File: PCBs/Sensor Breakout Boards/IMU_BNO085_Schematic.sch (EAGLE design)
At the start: 6 parts

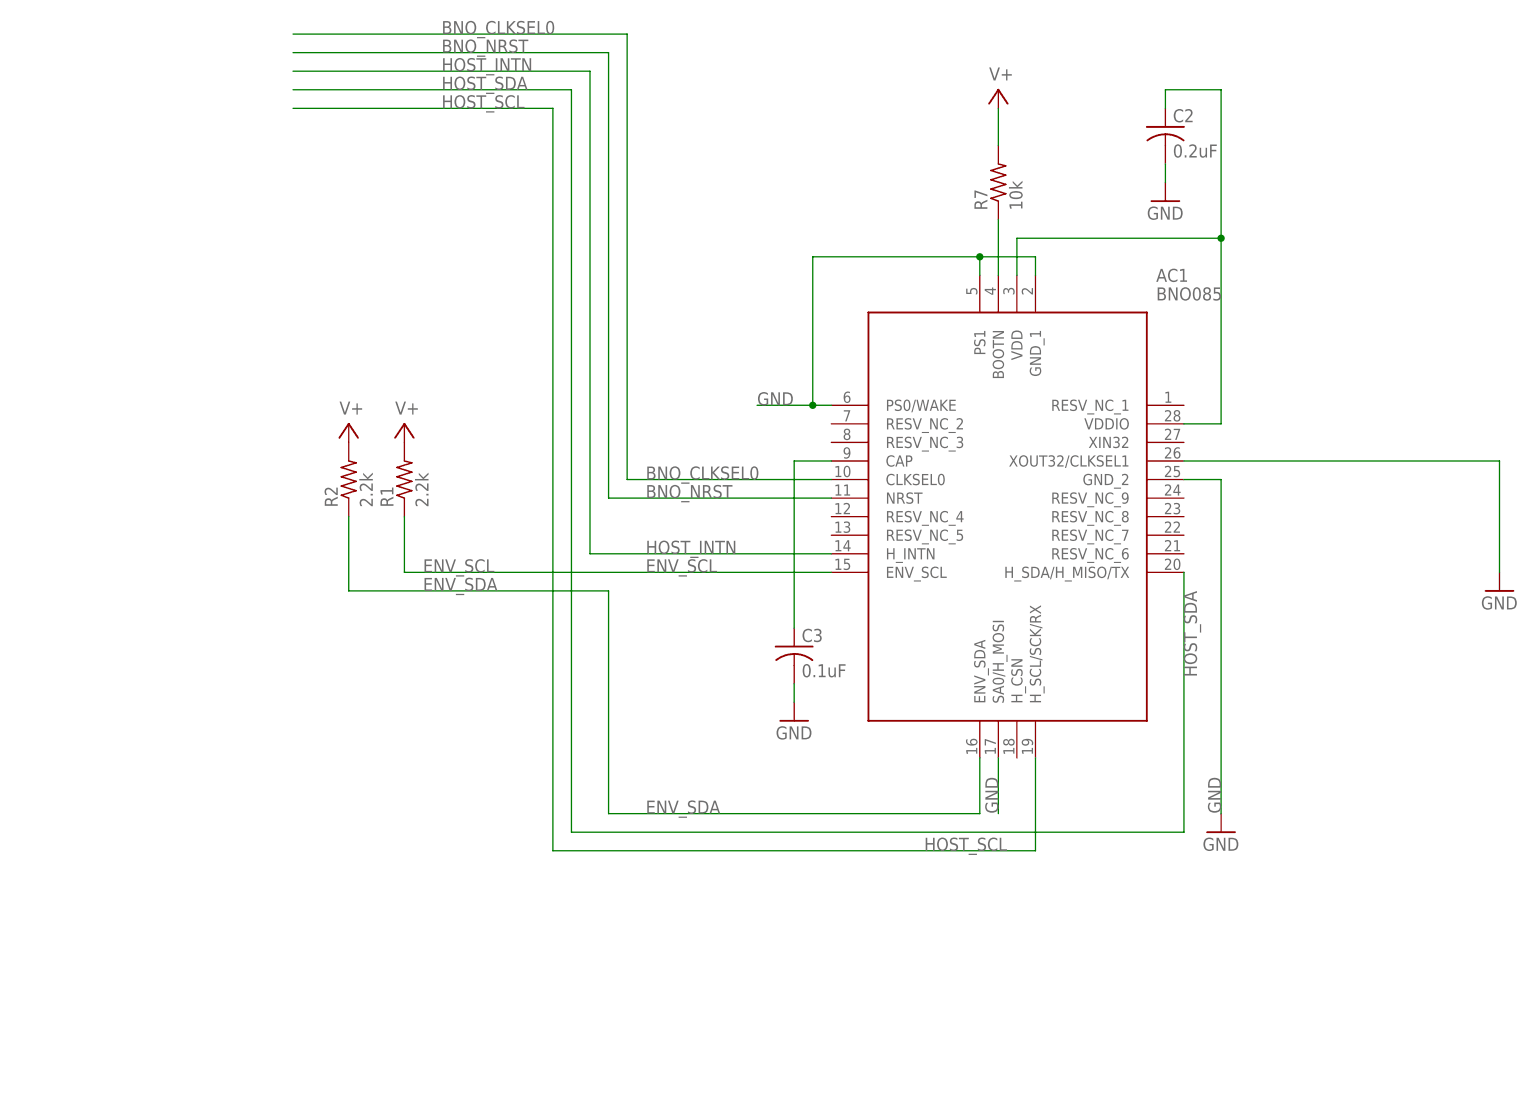
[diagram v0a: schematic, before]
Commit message: Revised IMU schematic and roughed out board
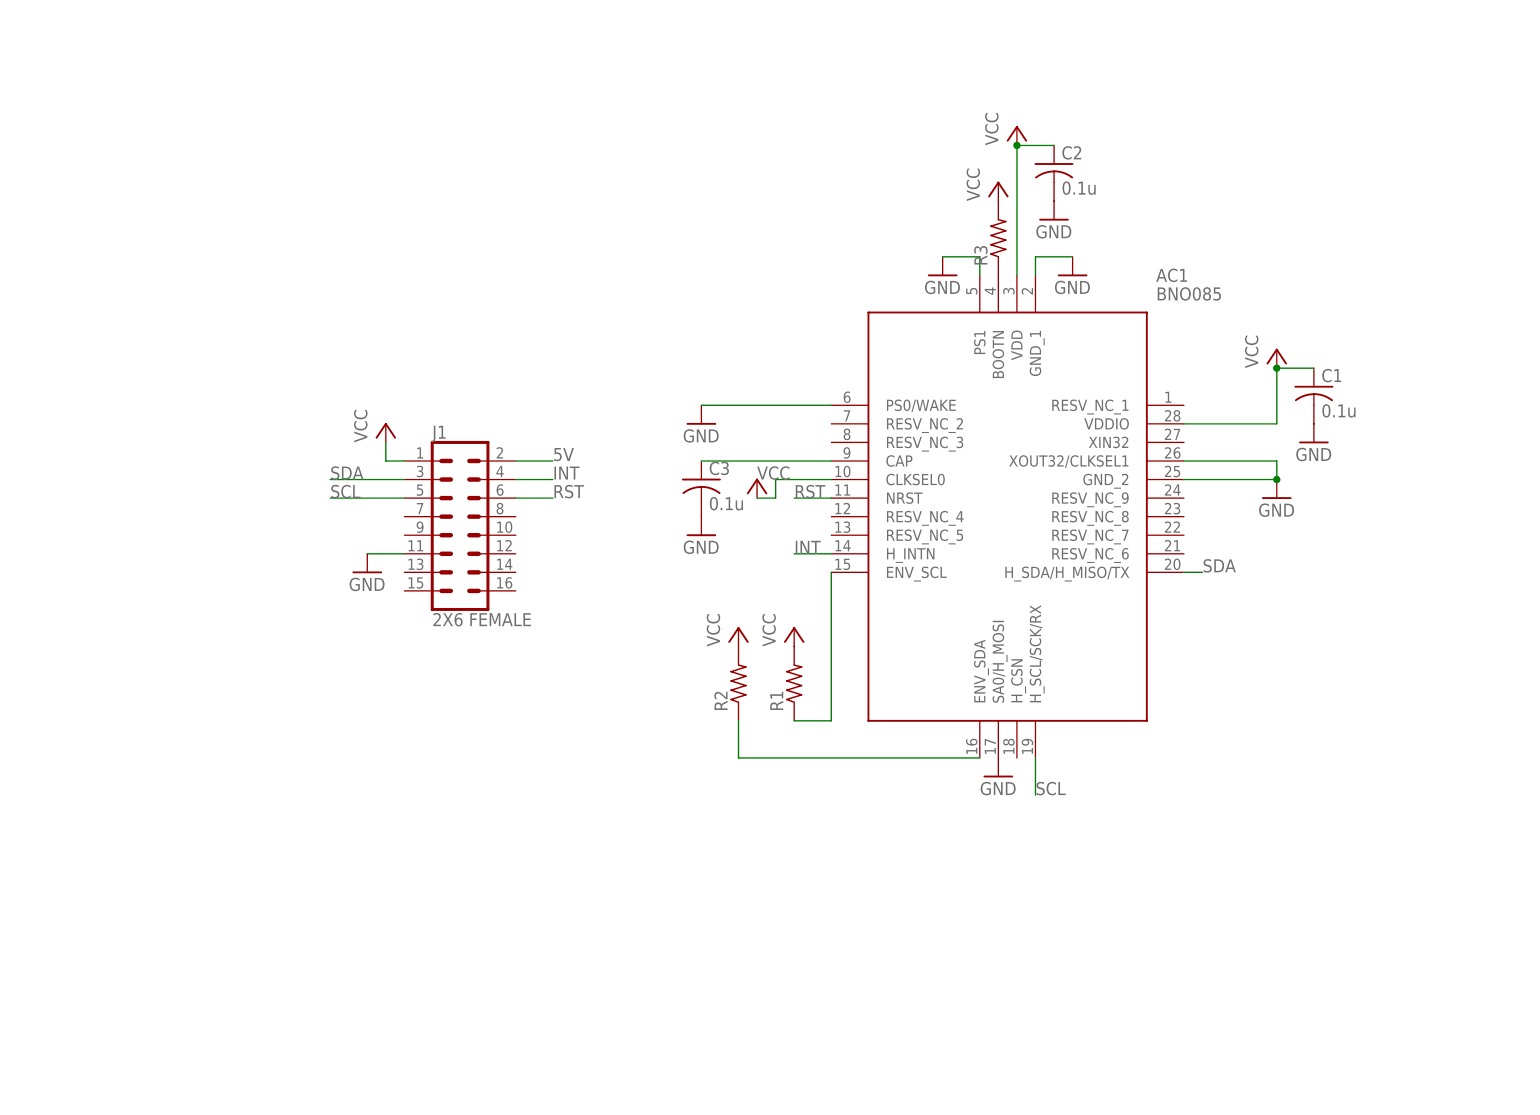
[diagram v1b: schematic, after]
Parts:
- removed R7: 10k, rcl:R-US_M0805
- added C1: 0.1u, RTR Main Library:C-ALL_PACKAGESC1206
- added J1: 2X6 FEMALE, RTR Main Library:SENSOR_BREAKOUTPTH_FEMALE
- added R3: (no value), RTR Main Library:R-ALL_PACKAGESR1206
- C2: value 0.2uF -> 0.1u; device rcl:C-US025-024X044 -> RTR Main Library:C-ALL_PACKAGESC1206
- C3: value 0.1uF -> 0.1u; device rcl:C-US025-024X044 -> RTR Main Library:C-ALL_PACKAGESC1206
- R1, R2: value 2.2k -> (none); device rcl:R-US_M0805 -> RTR Main Library:R-ALL_PACKAGESR1206
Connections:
- net ENV_SCL renamed N$4
- net ENV_SDA renamed N$5
- removed net BNO_CLKSEL0: AC1.CLKSEL0
- removed net BNO_NRST: AC1.NRST
- removed net HOST_INTN: AC1.H_INTN
- removed net HOST_SCL: AC1.H_SCL/SCK/RX
- removed net HOST_SDA: AC1.H_SDA/H_MISO/TX
- removed net N$3 (its old number): AC1.BOOTN, R7.1
- removed net V+: R1.2, R2.2, R7.2
- new net 5V: J1.2
- new net INT: AC1.H_INTN, J1.4
- new net RST: AC1.NRST, J1.6
- new net SCL: AC1.H_SCL/SCK/RX, J1.5
- new net SDA: AC1.H_SDA/H_MISO/TX, J1.3
- new net VCC: AC1.CLKSEL0, AC1.VDD, AC1.VDDIO, C1.1, C2.1, J1.1, R1.2, R2.2, R3.2
- net GND: now also C1.2, J1.11
- net N$1: now also AC1.BOOTN, R3.1; no longer AC1.VDD, AC1.VDDIO, C2.1
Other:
- moved on the sheet: C2, C3, R1, R2

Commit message: Laid out board + redid library for BNO
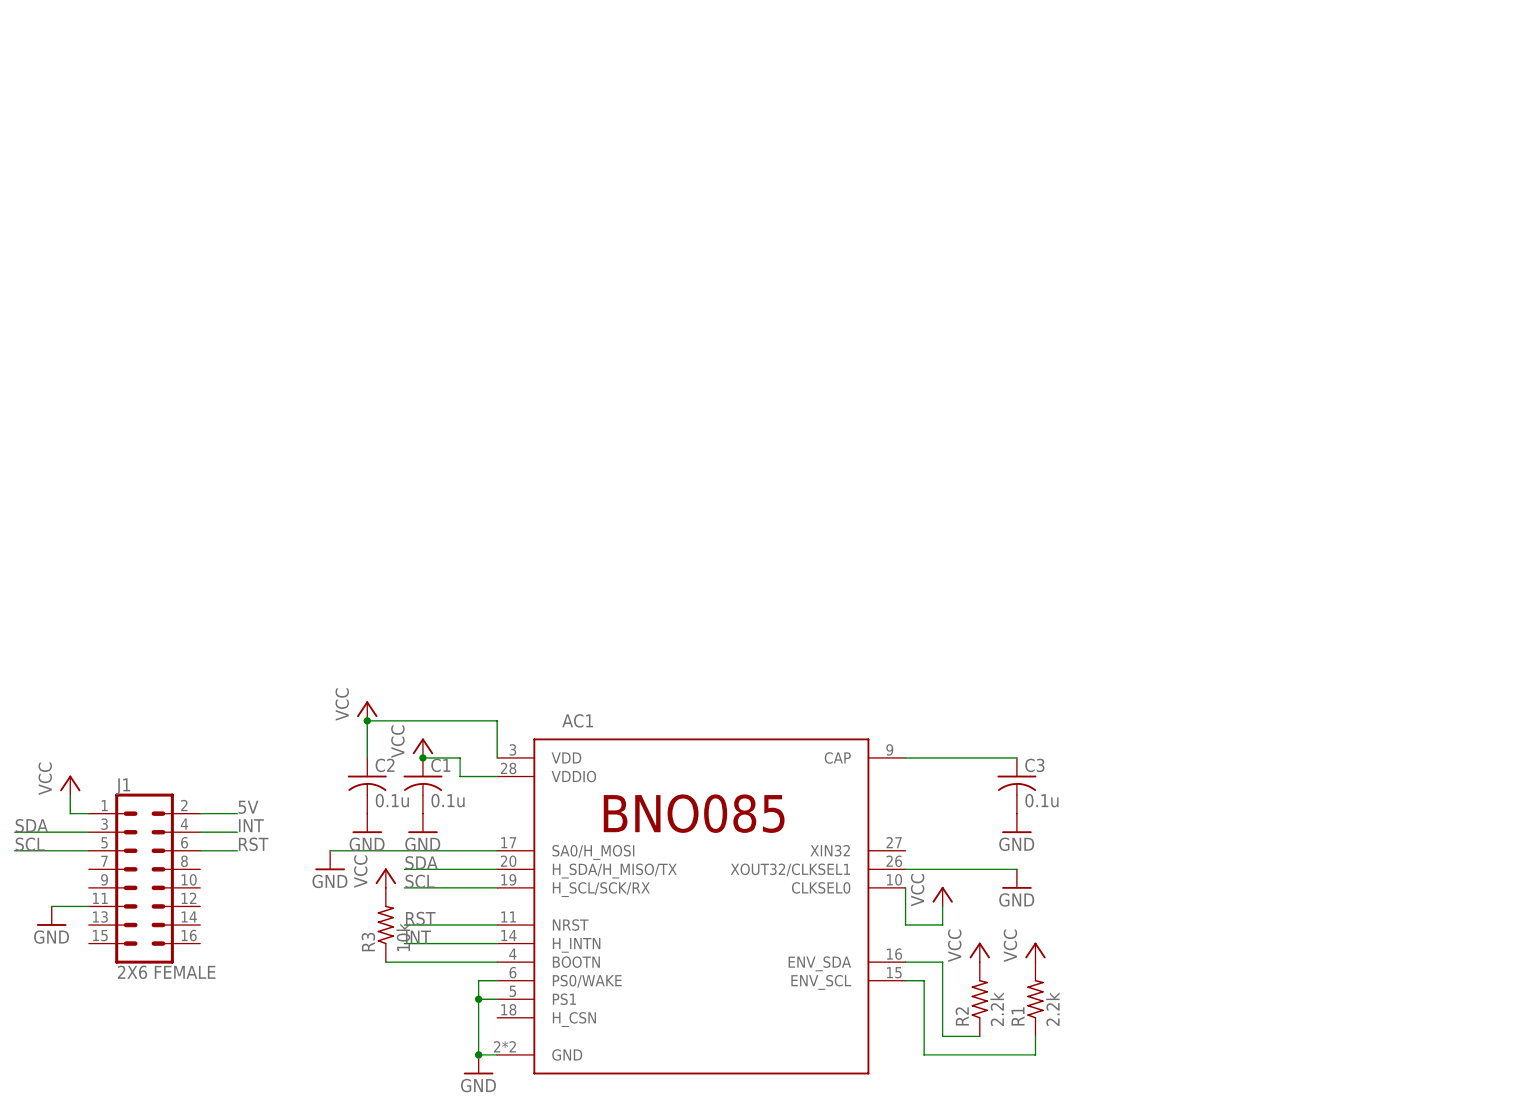
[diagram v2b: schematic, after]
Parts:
- R1, R2: value (none) -> 2.2k
- R3: value (none) -> 10k
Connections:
- net GND: now also AC1.GND; no longer AC1.GND_1, AC1.GND_2
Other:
- moved on the sheet: C1, C2, C3, J1, R1, R2, R3
